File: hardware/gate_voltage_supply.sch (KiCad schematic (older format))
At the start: 15 parts

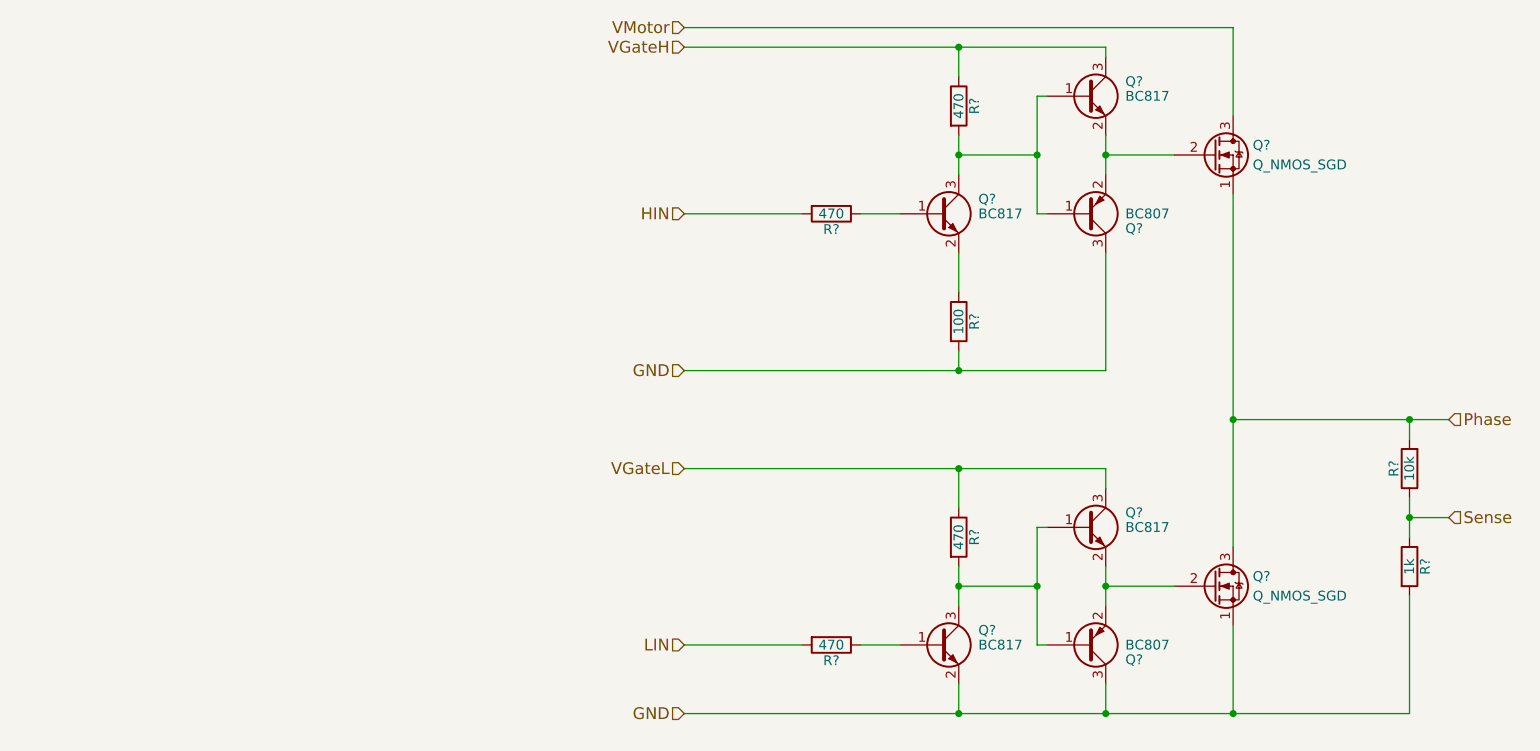
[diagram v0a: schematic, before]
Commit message: vgate, fet driver
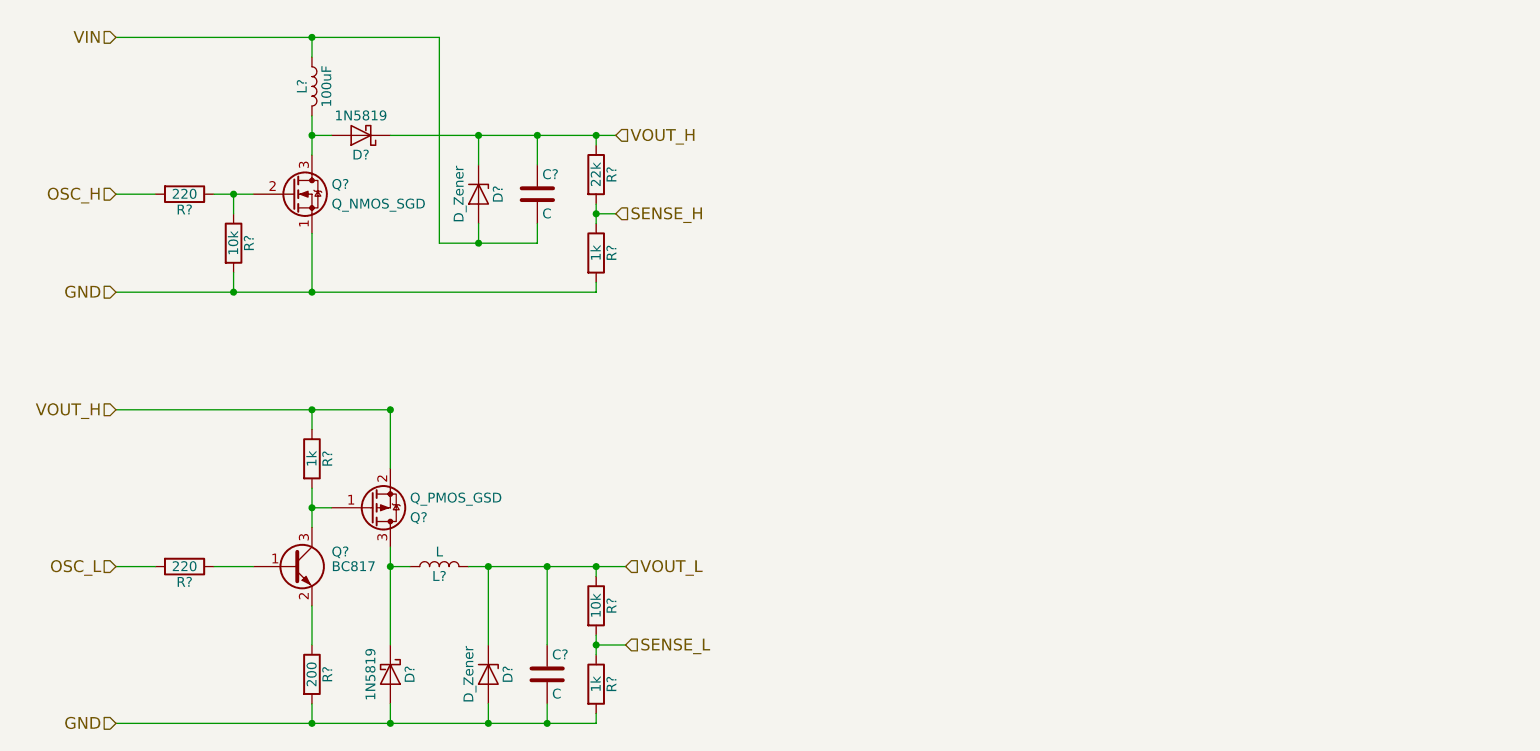
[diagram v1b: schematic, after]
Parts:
- removed Q? (x4): BC817, TO_SOT_Packages_SMD:SOT-23, symbol BC817
- removed Q? (x2): BC807, TO_SOT_Packages_SMD:SOT-23, symbol BC807
- removed Q? (x2): Q_NMOS_SGD, symbol Q_NMOS_SGD
- removed R? (x4): 470, symbol R
- removed R?: 100, symbol R
- removed R?: 10k, symbol R
- removed R?: 1k, symbol R
- added C? (x2): C, symbol C
- added D? (x2): 1N5819, Diodes_THT:D_DO-41_SOD81_Horizontal_RM10, symbol 1N5819
- added D? (x2): D_Zener, symbol D_Zener
- added L?: L, symbol L
- added L?: 100uF, symbol L
- added Q?: Q_NMOS_SGD, symbol Q_NMOS_SGD
- added Q?: BC817, TO_SOT_Packages_SMD:SOT-23, symbol BC817
- added Q?: Q_PMOS_GSD, symbol Q_PMOS_GSD
- added R? (x2): 220, symbol R
- added R? (x2): 10k, symbol R
- added R?: 200, symbol R
- added R? (x3): 1k, symbol R
- added R?: 22k, symbol R
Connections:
- net GND: now also C?.2, D?.2 (A), D?.2 (A), Q?.1 (S), R?.2, R?.2, R?.2, R?.2
- new net: Q?.1 (B), R?.1
- new net: D?.1 (K), L?.1, Q?.3 (D)
- new net: Q?.2 (G), R?.1, R?.1
- new net: D?.2 (A), L?.2, Q?.3 (D)
- new net: Q?.2 (E), R?.1
- new net: Q?.1 (G), Q?.3 (C), R?.2
- new net OSC_H: R?.2
- new net OSC_L: R?.2
- new net SENSE_H: R?.1, R?.2
- new net SENSE_L: R?.1, R?.2
- new net VIN: C?.2, D?.2 (A), L?.1
- new net VOUT_H: C?.1, D?.1 (K), D?.1 (K), Q?.2 (S), R?.1, R?.1
- new net VOUT_L: C?.1, D?.1 (K), L?.2, R?.1

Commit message: power, mcu
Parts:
- C5, C6: renamed from C?; footprint (none) -> Capacitors_SMD:C_0805
- D1, D2: renamed from D?; footprint Diodes_THT:D_DO-41_SOD81_Horizontal_RM10 -> Diodes_SMD:D_SOD-123
- D3, D4: renamed from D?; footprint (none) -> Diodes_SMD:D_MELF
- L1, L2: renamed from L?; footprint (none) -> Inductors:Inductor_Taiyo-Yuden_MD-3030
- Q33, Q35: renamed from Q?; footprint (none) -> TO_SOT_Packages_SMD:SOT-23
- R32, R33, R34, R35, R36, R37, R38, R39, R40: renamed from R?; footprint (none) -> Resistors_SMD:R_0603
- gave numbers to parts that had none: 1
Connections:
- net OSC_H renamed CLK_Vgh
- net OSC_L renamed CLK_Vgl
- net SENSE_H renamed SENSE_Vgh
- net SENSE_L renamed SENSE_Vgl
- net VOUT_H renamed Vgh
- net VOUT_L renamed Vgl

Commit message: phase routet
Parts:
- removed Q33: Q_NMOS_SGD, TO_SOT_Packages_SMD:SOT-23, symbol Q_NMOS_SGD
- added Q33: BSS138, TO_SOT_Packages_SMD:SOT-23, symbol Q_NMOS_GSD
- C17: renamed from C5; value C -> 22u
- C18: renamed from C6; value C -> 22u
- D1, D2: footprint Diodes_SMD:D_SOD-123 -> Diodes_SMD:D_SOD-323
- D3, D4: value D_Zener -> 18V; footprint Diodes_SMD:D_MELF -> Diodes_SMD:D_SOD-323
- L1: value 100uF -> 100u; footprint Inductors:Inductor_Taiyo-Yuden_MD-3030 -> gmcontrol:CD32
- L2: value L -> 100u; footprint Inductors:Inductor_Taiyo-Yuden_MD-3030 -> gmcontrol:CD32
- Q35: value Q_PMOS_GSD -> BSS84
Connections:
- net GND: now also Q33.2 (S)
- net at R32.1, R34.1: now also Q33.1 (G)
- net at D1.2 (A), L1.2: now also Q33.3 (D)
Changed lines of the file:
@@
 P 3800 3950
 F 0 "L2" V 3750 3950 50  0000 C CNN
-F 1 "L" V 3875 3950 50  0000 C CNN
-F 2 "Inductors:Inductor_Taiyo-Yuden_MD-3030" H 3800 3950 50  0001 C CNN
+F 1 "100u" V 3875 3950 50  0000 C CNN
+F 2 "gmcontrol:CD32" H 3800 3950 50  0001 C CNN
 F 3 "" H 3800 3950 50  0001 C CNN
 	1    3800 3950
@@
 F 0 "D2" H 3550 4600 50  0000 C CNN
 F 1 "1N5819" H 3550 4400 50  0000 C CNN
-F 2 "Diodes_SMD:D_SOD-123" H 3550 4325 50  0001 C CNN
+F 2 "Diodes_SMD:D_SOD-323" H 3550 4325 50  0001 C CNN
 F 3 "" H 3550 4500 50  0001 C CNN
 	1    3550 4500
@@
 P 4050 4500
 F 0 "D4" H 4050 4600 50  0000 C CNN
-F 1 "D_Zener" H 4050 4400 50  0000 C CNN
-F 2 "Diodes_SMD:D_MELF" H 4050 4500 50  0001 C CNN
+F 1 "18V" H 4050 4400 50  0000 C CNN
+F 2 "Diodes_SMD:D_SOD-323" H 4050 4500 50  0001 C CNN
 F 3 "" H 4050 4500 50  0001 C CNN
 	1    4050 4500
@@
 $EndComp
 $Comp
-L C C6
+L C C18
 U 1 1 5AE70D54
 P 4350 4500
-F 0 "C6" H 4375 4600 50  0000 L CNN
-F 1 "C" H 4375 4400 50  0000 L CNN
+F 0 "C18" H 4375 4600 50  0000 L CNN
+F 1 "22u" H 4375 4400 50  0000 L CNN
 F 2 "Capacitors_SMD:C_0805" H 4388 4350 50  0001 C CNN
 F 3 "" H 4350 4500 50  0001 C CNN
@@
 $EndComp
 $Comp
-L Q_NMOS_SGD Q33
-U 1 1 5AE8144D
-P 3050 2050
-F 0 "Q33" H 3250 2100 50  0000 L CNN
-F 1 "Q_NMOS_SGD" H 3250 2000 50  0000 L CNN
-F 2 "TO_SOT_Packages_SMD:SOT-23" H 3250 2150 50  0001 C CNN
-F 3 "" H 3050 2050 50  0001 C CNN
-	1    3050 2050
-	1    0    0    -1
-$EndComp
-$Comp
 L L L1
 U 1 1 5AE81454
 P 3150 1500
 F 0 "L1" V 3100 1500 50  0000 C CNN
-F 1 "100uF" V 3225 1500 50  0000 C CNN
-F 2 "Inductors:Inductor_Taiyo-Yuden_MD-3030" H 3150 1500 50  0001 C CNN
+F 1 "100u" V 3225 1500 50  0000 C CNN
+F 2 "gmcontrol:CD32" H 3150 1500 50  0001 C CNN
 F 3 "" H 3150 1500 50  0001 C CNN
 	1    3150 1500
@@
 F 0 "D1" H 3400 1850 50  0000 C CNN
 F 1 "1N5819" H 3400 1650 50  0000 C CNN
-F 2 "Diodes_SMD:D_SOD-123" H 3400 1575 50  0001 C CNN
+F 2 "Diodes_SMD:D_SOD-323" H 3400 1575 50  0001 C CNN
 F 3 "" H 3400 1750 50  0001 C CNN
 	1    3400 1750
@@
 P 4000 2050
 F 0 "D3" H 4000 2150 50  0000 C CNN
-F 1 "D_Zener" H 4000 1950 50  0000 C CNN
-F 2 "Diodes_SMD:D_MELF" H 4000 2050 50  0001 C CNN
+F 1 "18V" H 4000 1950 50  0000 C CNN
+F 2 "Diodes_SMD:D_SOD-323" H 4000 2050 50  0001 C CNN
 F 3 "" H 4000 2050 50  0001 C CNN
 	1    4000 2050
@@
 $EndComp
 $Comp
-L C C5
+L C C17
 U 1 1 5AE81469
 P 4300 2050
-F 0 "C5" H 4325 2150 50  0000 L CNN
-F 1 "C" H 4325 1950 50  0000 L CNN
+F 0 "C17" H 4325 2150 50  0000 L CNN
+F 1 "22u" H 4325 1950 50  0000 L CNN
 F 2 "Capacitors_SMD:C_0805" H 4338 1900 50  0001 C CNN
 F 3 "" H 4300 2050 50  0001 C CNN
@@
 P 3450 3650
 F 0 "Q35" H 3650 3700 50  0000 L CNN
-F 1 "Q_PMOS_GSD" H 3650 3600 50  0000 L CNN
+F 1 "BSS84" H 3650 3600 50  0000 L CNN
 F 2 "TO_SOT_Packages_SMD:SOT-23" H 3650 3750 50  0001 C CNN
 F 3 "" H 3450 3650 50  0001 C CNN
@@
 	4600 4350 4750 4350
 Connection ~ 4600 4350
+$Comp
+L Q_NMOS_GSD Q33
+U 1 1 5AE9B04D
+P 3050 2050
+F 0 "Q33" H 3250 2100 50  0000 L CNN
+F 1 "BSS138" H 3250 2000 50  0000 L CNN
+F 2 "TO_SOT_Packages_SMD:SOT-23" H 3250 2150 50  0001 C CNN
+F 3 "" H 3050 2050 50  0001 C CNN
+	1    3050 2050
+	1    0    0    -1
+$EndComp
 $EndSCHEMATC

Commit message: change to kicad 5
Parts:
- C17, C18: footprint Capacitors_SMD:C_0805 -> Capacitor_SMD:C_0805_2012Metric; symbol C -> Device:C
- D1, D2: footprint Diodes_SMD:D_SOD-323 -> Diode_SMD:D_SOD-323; symbol 1N5819 -> Diode:1N5819
- D3, D4: footprint Diodes_SMD:D_SOD-323 -> Diode_SMD:D_SOD-323; symbol D_Zener -> Device:D_Zener
- L1, L2: symbol L -> Device:L
- Q33: footprint TO_SOT_Packages_SMD:SOT-23 -> Package_TO_SOT_SMD:SOT-23; symbol Q_NMOS_GSD -> Device:Q_NMOS_GSD
- Q34: footprint TO_SOT_Packages_SMD:SOT-23 -> Package_TO_SOT_SMD:SOT-23; symbol BC817 -> Transistor_BJT:BC817
- Q35: footprint TO_SOT_Packages_SMD:SOT-23 -> Package_TO_SOT_SMD:SOT-23; symbol Q_PMOS_GSD -> Device:Q_PMOS_GSD
- R32, R33, R34, R35, R36, R37, R38, R39, R40: footprint Resistors_SMD:R_0603 -> Resistor_SMD:R_0603_1608Metric; symbol R -> Device:R

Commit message: smaller footprints
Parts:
- C17, C18: footprint Capacitor_SMD:C_0805_2012Metric -> _Generic:0805_Small
- Q33, Q34, Q35: footprint Package_TO_SOT_SMD:SOT-23 -> _Generic:SOT-23_Small
- R32, R33, R34, R35, R36, R37, R38, R39, R40: footprint Resistor_SMD:R_0603_1608Metric -> _Generic:0603_Small
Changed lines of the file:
@@
 F 0 "R33" V 2580 3950 50  0000 C CNN
 F 1 "220" V 2500 3950 50  0000 C CNN
-F 2 "Resistor_SMD:R_0603_1608Metric" V 2430 3950 50  0001 C CNN
+F 2 "_Generic:0603_Small" V 2430 3950 50  0001 C CNN
 F 3 "" H 2500 3950 50  0001 C CNN
 	1    2500 3950
@@
 F 0 "C18" H 4375 4600 50  0000 L CNN
 F 1 "22u" H 4375 4400 50  0000 L CNN
-F 2 "Capacitor_SMD:C_0805_2012Metric" H 4388 4350 50  0001 C CNN
+F 2 "_Generic:0805_Small" H 4388 4350 50  0001 C CNN
 F 3 "" H 4350 4500 50  0001 C CNN
 	1    4350 4500
@@
 F 0 "R32" V 2580 2050 50  0000 C CNN
 F 1 "220" V 2500 2050 50  0000 C CNN
-F 2 "Resistor_SMD:R_0603_1608Metric" V 2430 2050 50  0001 C CNN
+F 2 "_Generic:0603_Small" V 2430 2050 50  0001 C CNN
 F 3 "" H 2500 2050 50  0001 C CNN
 	1    2500 2050
@@
 F 0 "C17" H 4325 2150 50  0000 L CNN
 F 1 "22u" H 4325 1950 50  0000 L CNN
-F 2 "Capacitor_SMD:C_0805_2012Metric" H 4338 1900 50  0001 C CNN
+F 2 "_Generic:0805_Small" H 4338 1900 50  0001 C CNN
 F 3 "" H 4300 2050 50  0001 C CNN
 	1    4300 2050
@@
 F 0 "R34" V 2830 2300 50  0000 C CNN
 F 1 "10k" V 2750 2300 50  0000 C CNN
-F 2 "Resistor_SMD:R_0603_1608Metric" V 2680 2300 50  0001 C CNN
+F 2 "_Generic:0603_Small" V 2680 2300 50  0001 C CNN
 F 3 "" H 2750 2300 50  0001 C CNN
 	1    2750 2300
@@
 F 0 "Q34" H 3250 4025 50  0000 L CNN
 F 1 "BC817" H 3250 3950 50  0000 L CNN
-F 2 "Package_TO_SOT_SMD:SOT-23" H 3250 3875 50  0001 L CIN
+F 2 "_Generic:SOT-23_Small" H 3250 3875 50  0001 L CIN
 F 3 "" H 3050 3950 50  0001 L CNN
 	1    3050 3950
@@
 F 0 "R36" V 3230 4500 50  0000 C CNN
 F 1 "200" V 3150 4500 50  0000 C CNN
-F 2 "Resistor_SMD:R_0603_1608Metric" V 3080 4500 50  0001 C CNN
+F 2 "_Generic:0603_Small" V 3080 4500 50  0001 C CNN
 F 3 "" H 3150 4500 50  0001 C CNN
 	1    3150 4500
@@
 F 0 "Q35" H 3650 3700 50  0000 L CNN
 F 1 "BSS84" H 3650 3600 50  0000 L CNN
-F 2 "Package_TO_SOT_SMD:SOT-23" H 3650 3750 50  0001 C CNN
+F 2 "_Generic:SOT-23_Small" H 3650 3750 50  0001 C CNN
 F 3 "" H 3450 3650 50  0001 C CNN
 	1    3450 3650
@@
 F 0 "R35" V 3230 3400 50  0000 C CNN
 F 1 "1k" V 3150 3400 50  0000 C CNN
-F 2 "Resistor_SMD:R_0603_1608Metric" V 3080 3400 50  0001 C CNN
+F 2 "_Generic:0603_Small" V 3080 3400 50  0001 C CNN
 F 3 "" H 3150 3400 50  0001 C CNN
 	1    3150 3400
@@
 F 0 "R37" V 4680 1950 50  0000 C CNN
 F 1 "22k" V 4600 1950 50  0000 C CNN
-F 2 "Resistor_SMD:R_0603_1608Metric" V 4530 1950 50  0001 C CNN
+F 2 "_Generic:0603_Small" V 4530 1950 50  0001 C CNN
 F 3 "" H 4600 1950 50  0001 C CNN
 	1    4600 1950
@@
 F 0 "R38" V 4680 2350 50  0000 C CNN
 F 1 "1k" V 4600 2350 50  0000 C CNN
-F 2 "Resistor_SMD:R_0603_1608Metric" V 4530 2350 50  0001 C CNN
+F 2 "_Generic:0603_Small" V 4530 2350 50  0001 C CNN
 F 3 "" H 4600 2350 50  0001 C CNN
 	1    4600 2350
@@
 F 0 "R39" V 4680 4150 50  0000 C CNN
 F 1 "10k" V 4600 4150 50  0000 C CNN
-F 2 "Resistor_SMD:R_0603_1608Metric" V 4530 4150 50  0001 C CNN
+F 2 "_Generic:0603_Small" V 4530 4150 50  0001 C CNN
 F 3 "" H 4600 4150 50  0001 C CNN
 	1    4600 4150
@@
 F 0 "R40" V 4680 4550 50  0000 C CNN
 F 1 "1k" V 4600 4550 50  0000 C CNN
-F 2 "Resistor_SMD:R_0603_1608Metric" V 4530 4550 50  0001 C CNN
+F 2 "_Generic:0603_Small" V 4530 4550 50  0001 C CNN
 F 3 "" H 4600 4550 50  0001 C CNN
 	1    4600 4550
@@
 F 0 "Q33" H 3250 2100 50  0000 L CNN
 F 1 "BSS138" H 3250 2000 50  0000 L CNN
-F 2 "Package_TO_SOT_SMD:SOT-23" H 3250 2150 50  0001 C CNN
+F 2 "_Generic:SOT-23_Small" H 3250 2150 50  0001 C CNN
 F 3 "" H 3050 2050 50  0001 C CNN
 	1    3050 2050

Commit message: Ordered V1 PCB version
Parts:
- R36: value 200 -> 220
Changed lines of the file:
@@
 P 3150 4500
 F 0 "R36" V 3230 4500 50  0000 C CNN
-F 1 "200" V 3150 4500 50  0000 C CNN
+F 1 "220" V 3150 4500 50  0000 C CNN
 F 2 "_Generic:0603_Small" V 3080 4500 50  0001 C CNN
 F 3 "" H 3150 4500 50  0001 C CNN
